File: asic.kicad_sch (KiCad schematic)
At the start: 43 parts, among them U10 25MHz, U11 MCP1824T-1202E/OT, U12 MCP1824T-1202E/OT, U2 SN74AVC4T774, U7 MCP1824T-1202E/OT, U9 MCP1824T-1202E/OT

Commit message: made the board double wide. rough ASIC and vreg placement.
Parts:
- renumbered C60 to C46, C38 to C47, C183 to C49, C179 to C50, C184 to C51, C180 to C52, C181 to C53, C182 to C54, C177 to C55, C178 to C56, C64 to C57, C62 to C58, C55 to C60, C65 to C61, C63 to C62, C61 to C63, C56 to C64, R25 to R28, TP7 to TP14, TP8 to TP15, TP9 to TP16, TP10 to TP17, TP11 to TP18, TP29 to TP19, TP19 to TP20, TP18 to TP21, TP16 to TP22, U9 to U10, U7 to U11, U10 to U6, U2 to U7, U12 to U8, U11 to U9
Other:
- moved on the sheet: C47, C48, R28, U7

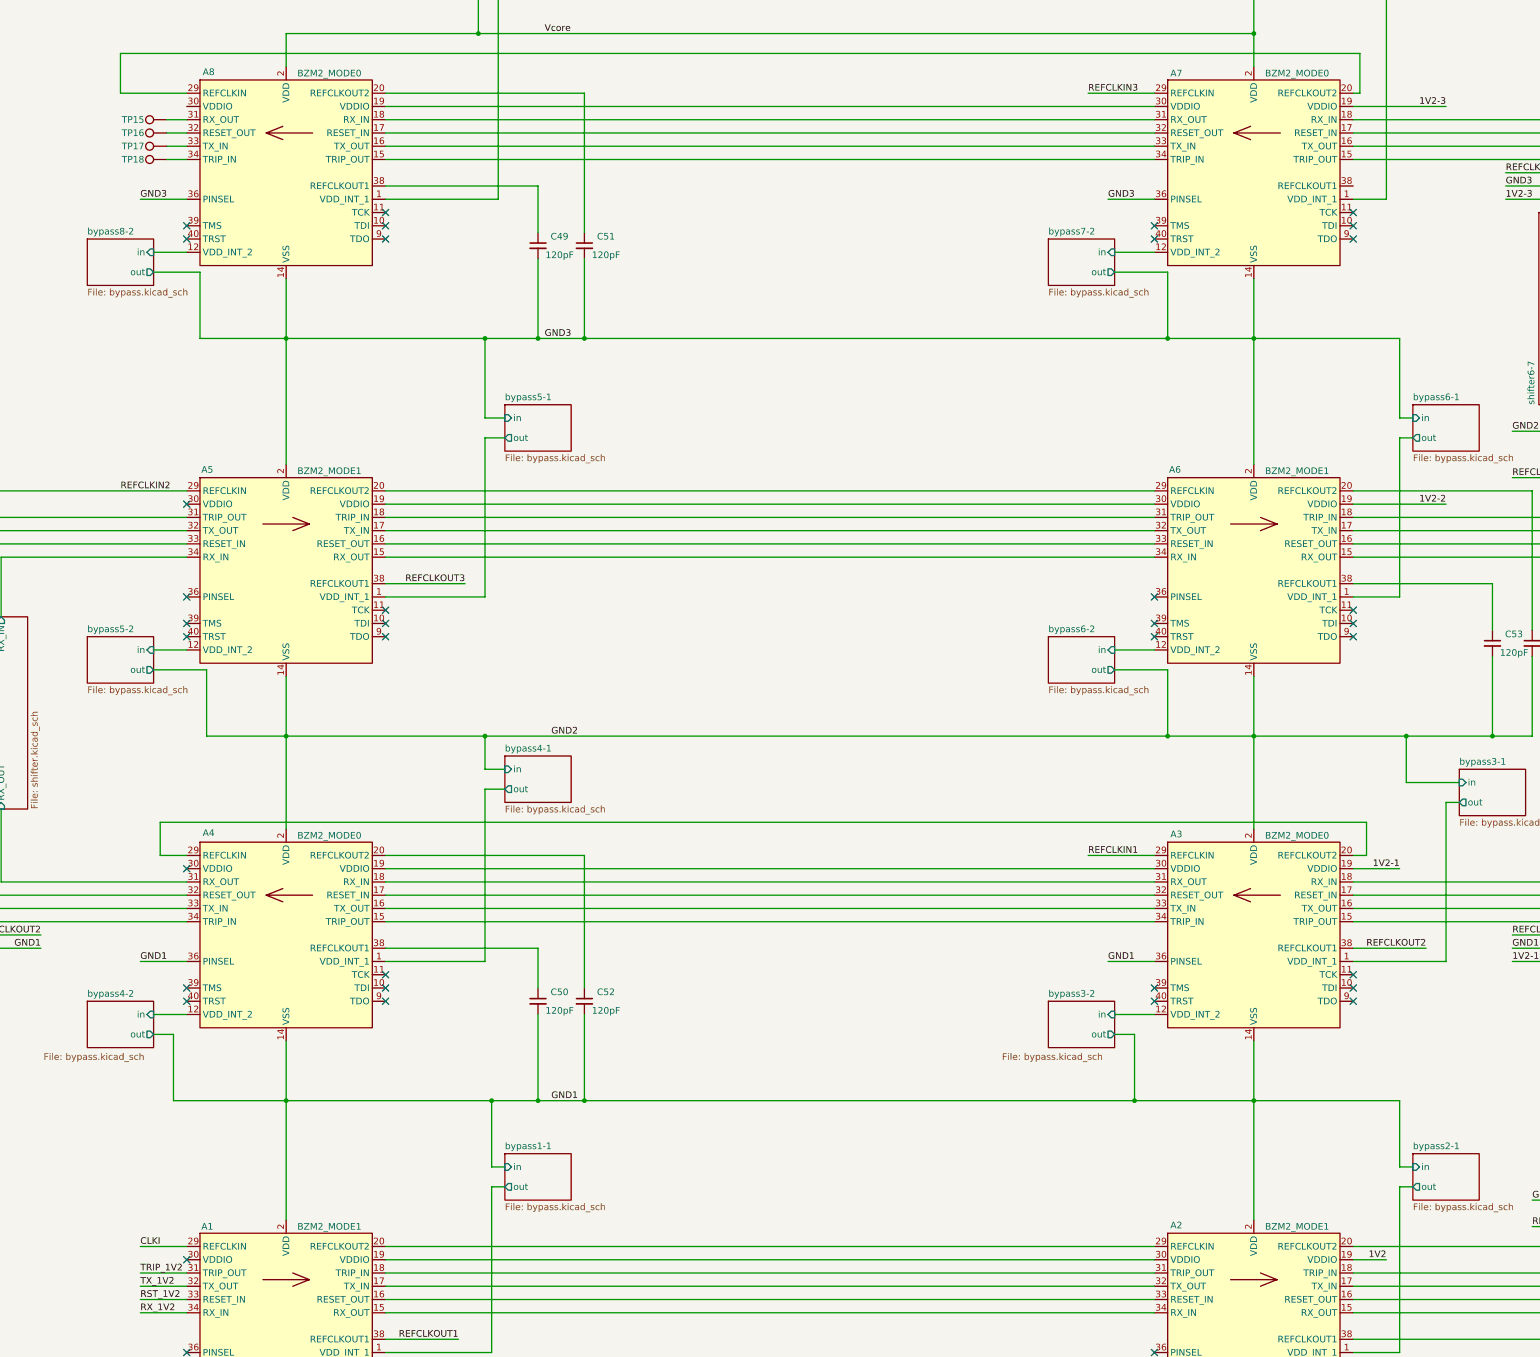
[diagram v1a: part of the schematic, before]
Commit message: ASICs placed. most other parts placed.
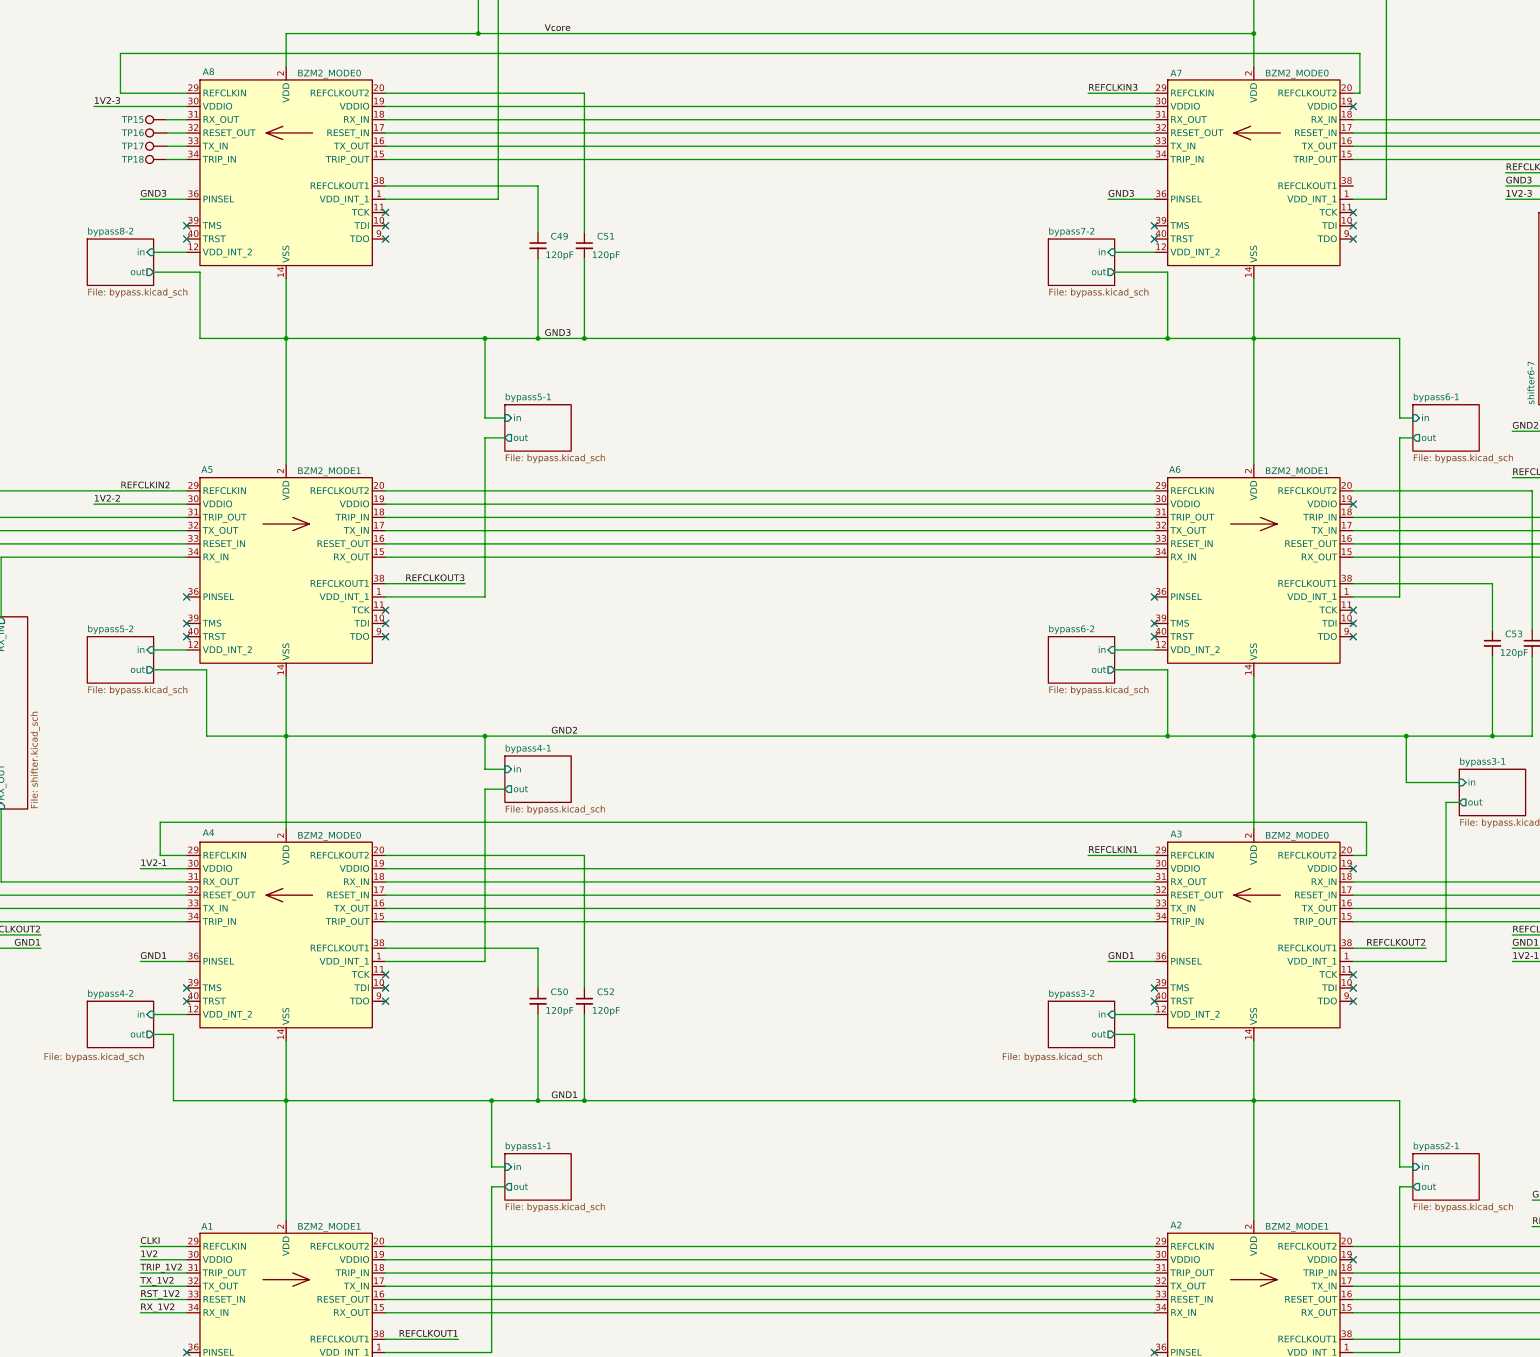
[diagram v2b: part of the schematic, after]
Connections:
- net 1V2: now also A1.30 (VDDIO); no longer A2.19 (VDDIO)
- net 1V2-1: now also A4.30 (VDDIO); no longer A3.19 (VDDIO)
- net 1V2-2: now also A5.30 (VDDIO); no longer A6.19 (VDDIO)
- net 1V2-3: now also A8.30 (VDDIO); no longer A7.19 (VDDIO)
- no-connect marks 51 -> 52
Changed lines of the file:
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@@
 	)
 	(no_connect
-		(at 171.45 247.65)
+		(at 394.97 247.65)
 	)
 	(no_connect
@@
 	)
 	(no_connect
+		(at 394.97 101.6)
+	)
+	(no_connect
 		(at 209.55 127)
 	)
@@
 	)
 	(no_connect
-		(at 171.45 322.58)
+		(at 394.97 322.58)
 	)
 	(no_connect
@@
 	)
 	(no_connect
-		(at 171.45 177.8)
+		(at 394.97 177.8)
 	)
 	(no_connect
@@
 	(wire
 		(pts
-			(xy 394.97 177.8) (xy 412.75 177.8)
+			(xy 171.45 177.8) (xy 153.67 177.8)
 		)
 		(stroke
@@
 	(wire
 		(pts
-			(xy 394.97 101.6) (xy 412.75 101.6)
+			(xy 171.45 101.6) (xy 153.67 101.6)
 		)
 		(stroke
@@
 	(wire
 		(pts
-			(xy 394.97 322.58) (xy 401.32 322.58)
+			(xy 171.45 322.58) (xy 162.56 322.58)
 		)
 		(stroke
@@
 	(wire
 		(pts
-			(xy 394.97 247.65) (xy 403.86 247.65)
+			(xy 171.45 247.65) (xy 162.56 247.65)
 		)
 		(stroke
@@
 	)
 	(label "1V2-2"
-		(at 412.75 177.8 180)
+		(at 153.67 177.8 0)
 		(effects
 			(font
 				(size 1.27 1.27)
 			)
-			(justify right bottom)
+			(justify left bottom)
 		)
 	)
@@
 	)
 	(label "1V2-1"
-		(at 403.86 247.65 180)
+		(at 162.56 247.65 0)
 		(effects
 			(font
 				(size 1.27 1.27)
 			)
-			(justify right bottom)
+			(justify left bottom)
 		)
 	)
@@
 	)
 	(label "1V2"
-		(at 401.32 322.58 180)
+		(at 162.56 322.58 0)
 		(effects
 			(font
 				(size 1.27 1.27)
 			)
-			(justify right bottom)
+			(justify left bottom)
 		)
 	)
@@
 	)
 	(label "1V2-3"
-		(at 412.75 101.6 180)
+		(at 153.67 101.6 0)
 		(effects
 			(font
 				(size 1.27 1.27)
 			)
-			(justify right bottom)
+			(justify left bottom)
 		)
 	)

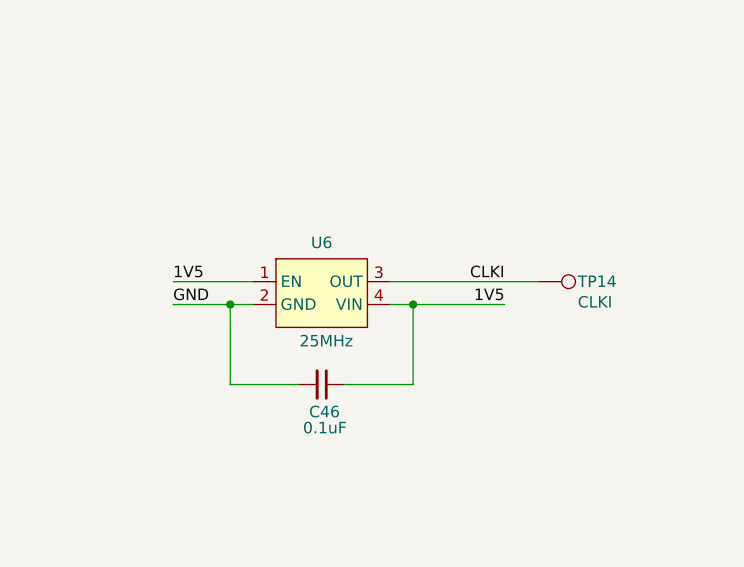
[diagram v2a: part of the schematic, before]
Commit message: routing is done. Power planes look good. DRC pass
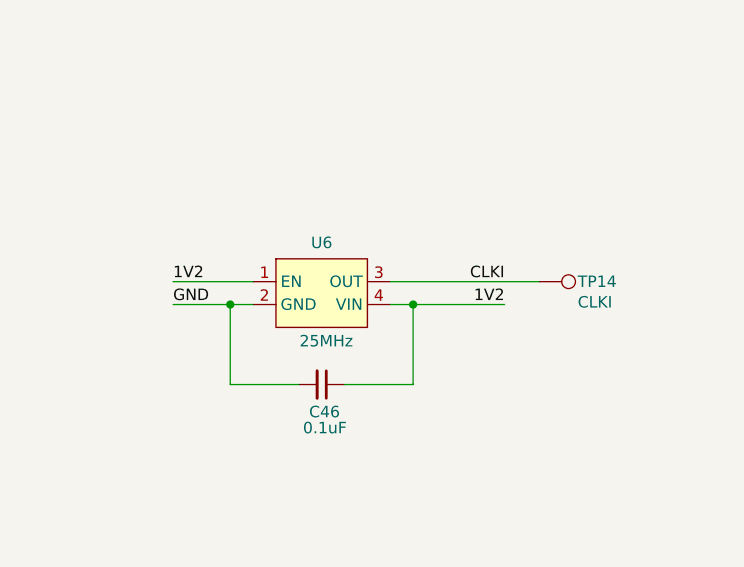
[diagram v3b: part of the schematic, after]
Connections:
- net 1V5 is gone; now on net 1V2: C46.1, U6.1 (EN), U6.4 (VIN)
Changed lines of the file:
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@@
 		)
 	)
-	(label "1V5"
+	(label "1V2"
 		(at 93.98 331.47 180)
 		(effects
@@
 		)
 	)
-	(label "1V5"
+	(label "1V2"
 		(at 57.15 328.93 0)
 		(effects

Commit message: switch to the bitaxeBIRDS based pre-bonanza
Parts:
- removed A2, A6: BZM2_MODE1, bitaxe:bzm2, symbol bitaxe:BZM2_mode1
- removed A3, A7: BZM2_MODE0, bitaxe:bzm2, symbol bitaxe:BZM2_mode0
- removed C46, C47, C48: 0.1uF, Capacitor_SMD:C_0402_1005Metric, symbol Device:C_Small
- removed C49, C50, C51, C52, C53, C54, C55, C56: 120pF, Capacitor_SMD:C_0402_1005Metric, symbol Device:C_Small
- removed TP15, TP16, TP18: CLKI, TestPoint:TestPoint_Pad_D1.0mm, symbol Connector:TestPoint
- removed TP19: 1V2, TestPoint:TestPoint_Pad_D1.5mm, symbol Connector:TestPoint
- removed U10, U11, U8, U9: MCP1824T-1202E/OT, Package_TO_SOT_SMD:SOT-23-5, symbol bitaxe:MCP1824
- removed U6: 25MHz, bitaxe:SMD3225-4P, symbol bitaxe:oscillator
- added C19, C25, C26, C27, C28, C68, C7, C72: 1uF, Capacitor_SMD:C_0402_1005Metric, symbol Device:C_Small
- added R4: 1k, Resistor_SMD:R_0402_1005Metric, symbol Device:R_Small_US
- added R9: 10k, Resistor_SMD:R_0402_1005Metric, symbol Device:R_Small_US
- added TP11, TP28, TP43: TTI, bitaxe:TestPoint_Pad_1.0x0.4mm, symbol Connector:TestPoint
- added TP12, TP29, TP44: TXI, bitaxe:TestPoint_Pad_1.0x0.4mm, symbol Connector:TestPoint
- added TP13, TP32, TP51, TP55, TP6: RSTI, bitaxe:TestPoint_Pad_1.0x0.4mm, symbol Connector:TestPoint
- added TP14, TP31, TP38, TP46: RXO, bitaxe:TestPoint_Pad_1.0x0.4mm, symbol Connector:TestPoint
- added TP2: 1V2-2, bitaxe:TestPoint_Pad_D1.0mm, symbol Connector:TestPoint
- added TP22: GND, bitaxe:TestPoint_Pad_1.0x0.4mm, symbol Connector:TestPoint
- added TP3: 1V2-3, bitaxe:TestPoint_Pad_D1.0mm, symbol Connector:TestPoint
- added TP30, TP39, TP45: RSTO, bitaxe:TestPoint_Pad_1.0x0.4mm, symbol Connector:TestPoint
- added TP33, TP40, TP50, TP54: TXO, bitaxe:TestPoint_Pad_1.0x0.4mm, symbol Connector:TestPoint
- added TP34, TP41, TP49, TP53: TTO, bitaxe:TestPoint_Pad_1.0x0.4mm, symbol Connector:TestPoint
- added TP35, TP48, TP57: CLKI, bitaxe:TestPoint_Pad_1.0x0.4mm, symbol Connector:TestPoint
- added TP36, TP52, TP56: RXI, bitaxe:TestPoint_Pad_1.0x0.4mm, symbol Connector:TestPoint
- added TP37, TP42, TP47: CLKO, bitaxe:TestPoint_Pad_1.0x0.4mm, symbol Connector:TestPoint
- added TP4: 1V2-4, bitaxe:TestPoint_Pad_D1.0mm, symbol Connector:TestPoint
- added TP58: D1, bitaxe:TestPoint_Pad_D1.0mm, symbol Connector:TestPoint
- added TP59: D2, bitaxe:TestPoint_Pad_D1.0mm, symbol Connector:TestPoint
- added TP60: D3, bitaxe:TestPoint_Pad_D1.0mm, symbol Connector:TestPoint
- added U1, U3, U4, U6: MCP1824T-1202E/OT, Package_TO_SOT_SMD:SOT-23-5, symbol bitaxe:MCP1824
- added Y2: 50MHz, bitaxe:OSC_ECS-3225MV-500-CN-TR, symbol bitaxe:oscillator
- A1: value BZM2_MODE1 -> BZM2_MODE0; symbol bitaxe:BZM2_mode1 -> bitaxe:BZM2_mode0
- A2: renamed from A4; value BZM2_MODE0 -> BZM2_MODE1; symbol bitaxe:BZM2_mode0 -> bitaxe:BZM2_mode1
- A3: renamed from A5; value BZM2_MODE1 -> BZM2_MODE0; symbol bitaxe:BZM2_mode1 -> bitaxe:BZM2_mode0
- A4: renamed from A8; value BZM2_MODE0 -> BZM2_MODE1; symbol bitaxe:BZM2_mode0 -> bitaxe:BZM2_mode1
- C57, C58, C59: value 1uF -> 0.1uF; DK 587-5514-1-ND -> 478-KGM05AR71C104KHCT-ND; PARTNO EMK105BJ105MV-F -> KGM05AR71C104KH
- C60, C61, C62, C63, C64: value 1uF -> 120pF; DK 587-5514-1-ND -> 490-16458-1-ND; PARTNO EMK105BJ105MV-F -> GCM1555C1H121FA16D
- TP10: renamed from TP14; footprint TestPoint:TestPoint_Pad_D1.0mm -> bitaxe:TestPoint_Pad_D1.0mm
- TP17: value CLKI -> TXO; footprint TestPoint:TestPoint_Pad_D1.0mm -> bitaxe:TestPoint_Pad_1.0x0.4mm
- TP18: renamed from TP22; value 1V2 -> 1V2-1; footprint TestPoint:TestPoint_Pad_D1.5mm -> bitaxe:TestPoint_Pad_D1.0mm; now left out of the parts list
- TP20: value 1V2 -> RXI; footprint TestPoint:TestPoint_Pad_D1.5mm -> bitaxe:TestPoint_Pad_1.0x0.4mm; now left out of the parts list
- TP21: value 1V2 -> TTO; footprint TestPoint:TestPoint_Pad_D1.5mm -> bitaxe:TestPoint_Pad_1.0x0.4mm; now left out of the parts list
- U8: renamed from U7; value SN74AVC4T774 -> SN74AXC4T774; Partnum (none) -> SN74AXC4T774BQBR
- renumbered R28 to R26
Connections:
- net CLKI is gone; now on net REFCLKIN1: A1.29 (REFCLKIN), TP10.1
- net bypass5-1/out is gone; now on net bypass3-1/out: A3.1 (VDD_INT_1)
- net bypass5-2/in is gone; now on net bypass3-2/in: A3.12 (VDD_INT_2)
- net bypass8-1/out is gone; now on net bypass4-1/out: A4.1 (VDD_INT_1)
- net bypass8-2/in is gone; now on net bypass4-2/in: A4.12 (VDD_INT_2)
- net 1V2-1: now also A1.30 (VDDIO), C57.1, C58.1, TP18.1, U8.16 (VCCA), U8.2 (DIR2), U8.8 (DIR4), C72.2, U6.5 (VOUT), Y2.1 (EN), Y2.4 (VIN); no longer A2.30 (VDDIO), C63.2, TP21.1
- net 1V2-2: now also A2.30 (VDDIO), C19.2, TP2.1, U1.5 (VOUT); no longer A3.30 (VDDIO), C62.2, TP20.1
- net 1V2-3: now also A3.30 (VDDIO), C26.2, TP3.1, U3.5 (VOUT); no longer A4.30 (VDDIO), C61.2
- net 3V3: now also C59.1
- net GND: now also A1.36 (PINSEL), C57.2, C58.2, C59.2, C64.2, U8.7 (DIR3), C68.1, C72.1, TP22.1, U6.2 (GND), Y2.2 (GND); no longer C60.1, C64.1, U8.2 (DIR2)
- net REFCLKIN1: now also Y2.3 (OUT)
- net REFCLKIN2: now also A2.29 (REFCLKIN), TP35.1; no longer A3.29 (REFCLKIN)
- net REFCLKIN3: now also A3.29 (REFCLKIN), TP57.1
- net REFCLKOUT1: now also TP37.1
- net REFCLKOUT2: now also A2.38 (REFCLKOUT1), TP42.1
- net REFCLKOUT3: now also TP47.1
- net RST_1V2: now also A1.17 (RESET_IN), TP6.1; no longer A1.33 (RESET_IN)
- net RX_1V2: now also A1.18 (RX_IN), TP20.1; no longer A1.34 (RX_IN)
- net TRIP_1V2: now also A1.15 (TRIP_OUT), TP21.1; no longer A1.31 (TRIP_OUT)
- net TX_1V2: now also A1.16 (TX_OUT), TP17.1; no longer A1.32 (TX_OUT)
- net bypass2-1/out: now also A2.1 (VDD_INT_1)
- net bypass2-2/in: now also A2.12 (VDD_INT_2)
- net bypass4-1/out: no longer A2.1 (VDD_INT_1)
- net bypass4-2/in: no longer A2.12 (VDD_INT_2)
- net shifter2-3/RESET_IN: now also A3.17 (RESET_IN), TP55.1
- net shifter2-3/RESET_OUT: now also A2.16 (RESET_OUT), TP39.1
- net shifter2-3/RX_IN: now also A3.18 (RX_IN), TP56.1
- net shifter2-3/RX_OUT: now also A2.15 (RX_OUT), TP38.1
- net shifter2-3/TRIP_IN: now also A2.18 (TRIP_IN), TP41.1
- net shifter2-3/TRIP_OUT: now also A3.15 (TRIP_OUT), TP53.1
- net shifter2-3/TX_IN: now also A2.17 (TX_IN), TP40.1
- net shifter2-3/TX_OUT: now also A3.16 (TX_OUT), TP54.1
- net at A2.20 (REFCLKOUT2): now also C63.1
- net shifter3-4/RX_IN: now reaches A4.34 (RX_IN)
- net shifter3-4/RX_IN: now also TP52.1
- net REFCLKIN4: now reaches A4.29 (REFCLKIN)
- net REFCLKIN4: now also TP48.1
- net at A4.18 (TRIP_IN): now also R9.1, TP11.1
- net at A4.17 (TX_IN): now also R4.2, TP12.1
- net at A4.16 (RESET_OUT): now also TP13.1
- net at A4.15 (RX_OUT): now also TP14.1
- net at A1.20 (REFCLKOUT2): now also C64.1
- net at A3.20 (REFCLKOUT2): now also C62.1
- net at A4.20 (REFCLKOUT2): now also C61.1
- net at A4.38 (REFCLKOUT1): now also C60.1
- net DOMAIN1: now reaches A3.36 (PINSEL)
- net DOMAIN1: now also A1.2 (VDD), A1.3 (VDD), A1.4 (VDD), A1.41 (VDD), A1.42 (VDD), A1.49 (VDD), A1.5 (VDD), A1.50 (VDD), A1.51 (VDD), A1.52 (VDD), A1.59 (VDD), A1.6 (VDD), A1.60 (VDD), A1.7 (VDD), A1.8 (VDD), A2.14 (VSS), A2.21 (VSS), A2.22 (VSS), A2.23 (VSS), A2.24 (VSS), A2.25 (VSS), A2.26 (VSS), A2.27 (VSS), A2.28 (VSS), A2.35 (VSS), A2.43 (VSS), A2.44 (VSS), A2.45 (VSS), A2.46 (VSS), A2.47 (VSS), A2.48 (VSS), A2.53 (VSS), A2.54 (VSS), A2.55 (VSS), A2.56 (VSS), A2.57 (VSS), A2.58 (VSS), C63.2, C19.1, C7.1, TP58.1, U1.2 (GND)
- net shifter3-4/TRIP_OUT: now reaches A4.31 (TRIP_OUT)
- net shifter3-4/TRIP_OUT: now also TP49.1
- net shifter3-4/TX_OUT: now reaches A4.32 (TX_OUT)
- net shifter3-4/TX_OUT: now also TP50.1
- net shifter3-4/RESET_IN: now reaches A4.33 (RESET_IN)
- net shifter3-4/RESET_IN: now also TP51.1; no longer TP17.1
- removed net 1V2: A1.30 (VDDIO), C64.2, TP18.1, U8.16 (VCCA), U8.7 (DIR3), U8.8 (DIR4)
- removed net 5V: C57.2, C58.2, C59.2, C60.2
- removed net GND1: A1.2 (VDD), A1.3 (VDD), A1.4 (VDD), A1.41 (VDD), A1.42 (VDD), A1.49 (VDD), A1.5 (VDD), A1.50 (VDD), A1.51 (VDD), A1.52 (VDD), A1.59 (VDD), A1.6 (VDD), A1.60 (VDD), A1.7 (VDD), A1.8 (VDD), A2.14 (VSS), A2.21 (VSS), A2.22 (VSS), A2.23 (VSS), A2.24 (VSS), A2.25 (VSS), A2.26 (VSS), A2.27 (VSS), A2.28 (VSS), A2.35 (VSS), A2.36 (PINSEL), A2.43 (VSS), A2.44 (VSS), A2.45 (VSS), A2.46 (VSS), A2.47 (VSS), A2.48 (VSS), A2.53 (VSS), A2.54 (VSS), A2.55 (VSS), A2.56 (VSS), A2.57 (VSS), A2.58 (VSS), C59.1, C63.1
- net GND2 renamed DOMAIN2
- net DOMAIN2: now also C62.2, C25.1, C26.1, TP59.1, U3.2 (GND); no longer C58.1, C62.1
- net GND3 renamed DOMAIN3
- net DOMAIN3: now also C60.2, C61.2, C27.1, C28.1, R9.2, TP60.1, U4.2 (GND); no longer A4.36 (PINSEL), C57.1, C61.1
- net TT_3V3 renamed TRIP_3V3
- net Vcore renamed VDD
- net shifter4-5/RESET_IN renamed shifter3-4/TX_IN
- net shifter3-4/TX_IN: now also TP44.1
- net shifter4-5/RESET_OUT renamed shifter1-2/TX_OUT
- net shifter1-2/TX_OUT: now also TP33.1
- net shifter4-5/RX_IN renamed shifter3-4/TRIP_IN
- net shifter3-4/TRIP_IN: now also TP43.1
- net shifter4-5/RX_OUT renamed shifter1-2/TRIP_OUT
- net shifter1-2/TRIP_OUT: now also TP34.1
- net shifter4-5/TRIP_IN renamed shifter1-2/RX_IN
- net shifter1-2/RX_IN: now also TP36.1
- net shifter4-5/TRIP_OUT renamed shifter3-4/RX_OUT
- net shifter3-4/RX_OUT: now also TP46.1
- net shifter4-5/TX_IN renamed shifter1-2/RESET_IN
- net shifter1-2/RESET_IN: now also TP32.1
- net shifter4-5/TX_OUT renamed shifter3-4/RESET_OUT
- net shifter3-4/RESET_OUT: now also TP45.1
- new net 1V2-4: A4.30 (VDDIO), C28.2, R4.1, TP4.1, U4.5 (VOUT)
- new net 5V_SWITCH: C25.2, C27.2, C68.2, C7.2, U1.1 (VIN), U1.3 (EN), U3.1 (VIN), U3.3 (EN), U4.1 (VIN), U4.3 (EN), U6.1 (VIN), U6.3 (EN)
- new net shifter1-2/RESET_OUT: A1.32 (RESET_OUT), TP30.1
- new net shifter1-2/RX_OUT: A1.31 (RX_OUT), TP31.1
- new net shifter1-2/TRIP_IN: A1.34 (TRIP_IN), TP28.1
- new net shifter1-2/TX_IN: A1.33 (TX_IN), TP29.1
- no-connect marks 52 -> 30
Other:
- removed sheet bypass5-1
- removed sheet bypass5-2
- removed sheet bypass6-1
- removed sheet bypass6-2
- removed sheet bypass7-1
- removed sheet bypass7-2
- removed sheet bypass8-1
- removed sheet bypass8-2
- removed sheet shifter4-5
- removed sheet shifter6-7
- added sheet shifter1-2 (shifter.kicad_sch)
- added sheet shifter3-4 (shifter.kicad_sch)
- sheet shifter2-3 ports: added GND_H, GND_L; removed GND0, GND1
- note added: "->"
- note added: "<-"
- note added: "DOMAIN 1"
- note added: "DOMAIN 2"
- note added: "DOMAIN 3"
- note added: "DOMAIN 4"
- moved on the sheet: A1, A2, A3, A4, R26, TP10, TP18, U8

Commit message: updated schematic worksheet
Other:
- company: (none) -> bitaxeorg
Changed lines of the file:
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@@
 		(date "2026-02-11")
 		(rev "1002x")
+		(company "bitaxeorg")
+		(comment 1 "OHL v2")
 	)
 	(text "->"

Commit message: changed TPS82130 voltage regulators to TPSM82903. Connected ESP32<->RP2040 CTRL serial port. made top mounting holes plated.
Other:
- moved on the sheet: C57, C59, R26, TP17, TP20, TP21, TP22, TP6, U8

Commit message: switched back to TPS82130. added BOM partnumbers
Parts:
- C19, C25, C26, C27, C28, C68, C7, C72: LCSC (none) -> C52923
- C57, C58, C59: LCSC (none) -> C307331
